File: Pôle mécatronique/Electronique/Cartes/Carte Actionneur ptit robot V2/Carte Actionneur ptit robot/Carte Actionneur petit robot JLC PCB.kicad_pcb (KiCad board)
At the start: 2 copper layers, 63 x 79 mm, 43 parts, among them Q1 BC557, U1 MCP2551-I-P

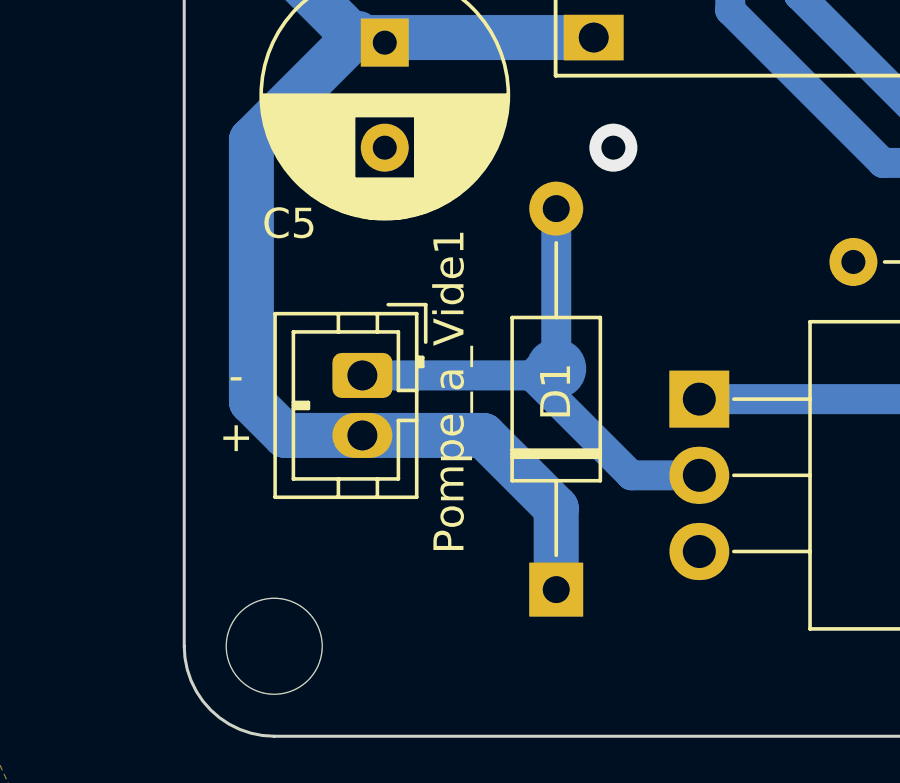
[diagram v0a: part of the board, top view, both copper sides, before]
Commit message: Update actionneur grand robot
Ajout d'une 2e empreinte avec détrompeur
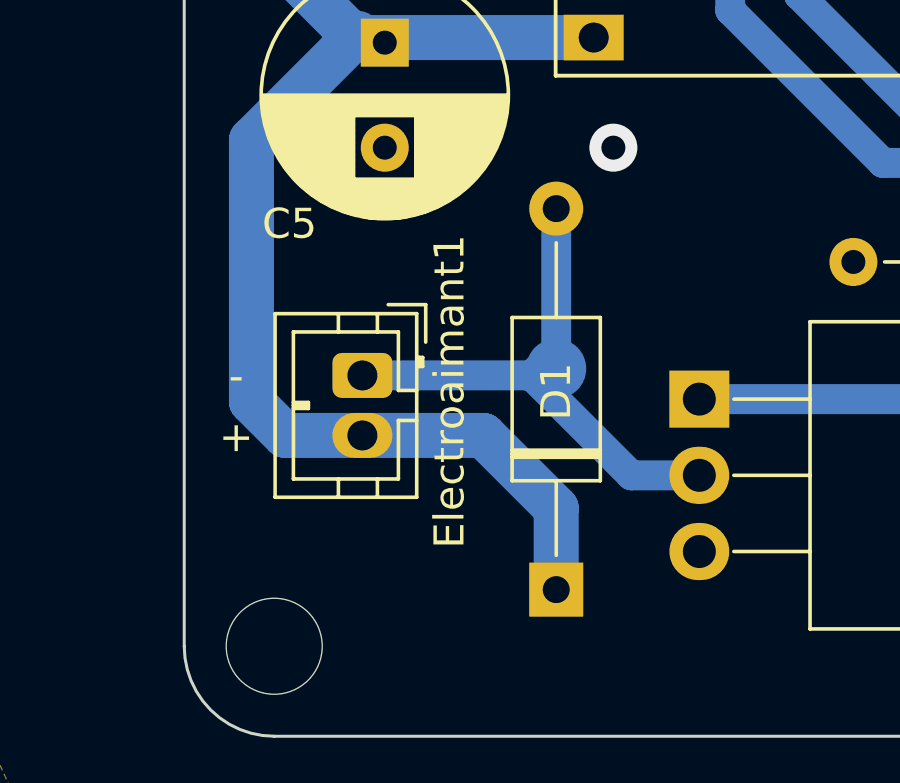
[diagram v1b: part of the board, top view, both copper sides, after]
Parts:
- renumbered Pompe_a_Vide1 to Electroaimant1
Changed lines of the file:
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@@
   (net 40 "unconnected-(U1-Pad5)")
   (net 41 "Net-(Q1-Pad1)")
-  (net 42 "Net-(R3-Pad1)")
+  (net 42 "Net-(Q1-Pad2)")
   (footprint "Connector_PinSocket_2.54mm:PinSocket_1x02_P2.54mm_Vertical" (layer "F.Cu")
     (at 175.006 69.596)
@@
     (property "Sheetname" "")
     (attr through_hole)
-    (fp_text reference "Pompe_a_Vide1" (at 0.535 -2.905 90) (layer "F.SilkS")
+    (fp_text reference "Electroaimant1" (at 0.535 -2.905 90) (layer "F.SilkS")
       (effects (font (size 1 1) (thickness 0.15)))
     )
@@
     (fp_line (start 8.23 -1.25) (end 1.93 -1.25) (layer "F.Fab") (width 0.1))
     (pad "1" thru_hole circle locked (at 0 0) (size 1.6 1.6) (drill 0.8) (layers *.Cu *.Mask)
-      (net 42 "Net-(R3-Pad1)") (pintype "passive"))
+      (net 42 "Net-(Q1-Pad2)") (pintype "passive"))
     (pad "2" thru_hole oval locked (at 10.16 0) (size 1.6 1.6) (drill 0.8) (layers *.Cu *.Mask)
       (net 5 "+5V") (pintype "passive"))
@@
       (net 41 "Net-(Q1-Pad1)") (pinfunction "C") (pintype "passive"))
     (pad "2" thru_hole oval locked (at 1.27 0 270) (size 1.05 1.5) (drill 0.75) (layers *.Cu *.Mask)
-      (net 42 "Net-(R3-Pad1)") (pinfunction "B") (pintype "input"))
+      (net 42 "Net-(Q1-Pad2)") (pinfunction "B") (pintype "input"))
     (pad "3" thru_hole oval locked (at 2.54 0 270) (size 1.05 1.5) (drill 0.75) (layers *.Cu *.Mask)
       (net 5 "+5V") (pinfunction "E") (pintype "passive"))
@@
     (fp_line (start 8.23 -1.25) (end 1.93 -1.25) (layer "F.Fab") (width 0.1))
     (pad "1" thru_hole circle locked (at 0 0 90) (size 1.6 1.6) (drill 0.8) (layers *.Cu *.Mask)
-      (net 42 "Net-(R3-Pad1)") (pintype "passive"))
+      (net 42 "Net-(Q1-Pad2)") (pintype "passive"))
     (pad "2" thru_hole oval locked (at 10.16 0 90) (size 1.6 1.6) (drill 0.8) (layers *.Cu *.Mask)
       (net 36 "AIMANT") (pintype "passive"))
@@
     (fp_circle (center 0 0) (end 1.5 0) (layer "B.CrtYd") (width 0.05) (fill none))
     (pad "1" smd circle locked (at 0 0 180) (size 2 2) (layers "B.Cu" "B.Mask")
-      (net 42 "Net-(R3-Pad1)") (pinfunction "1") (pintype "passive"))
+      (net 42 "Net-(Q1-Pad2)") (pinfunction "1") (pintype "passive"))
   )
   (footprint "TestPoint:TestPoint_Pad_D2.0mm" (layer "B.Cu")
